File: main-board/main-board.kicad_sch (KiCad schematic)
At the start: 60 parts, among them J1 Conn_02x08_Odd_Even, J2 7-12V, Q1 2N7000, Q2 2N7000, Q3 2N7000, Q4 2N7000, Q5 2N7000, Q6 2N7000, Q7 2N7000, Q8 2N7000, Q9 2N3904, U1 40106, U2 4024, U3 4040, U4 27C256, U5 LM78L05, U6 ULN2803A, U7 4028, U9 L7805

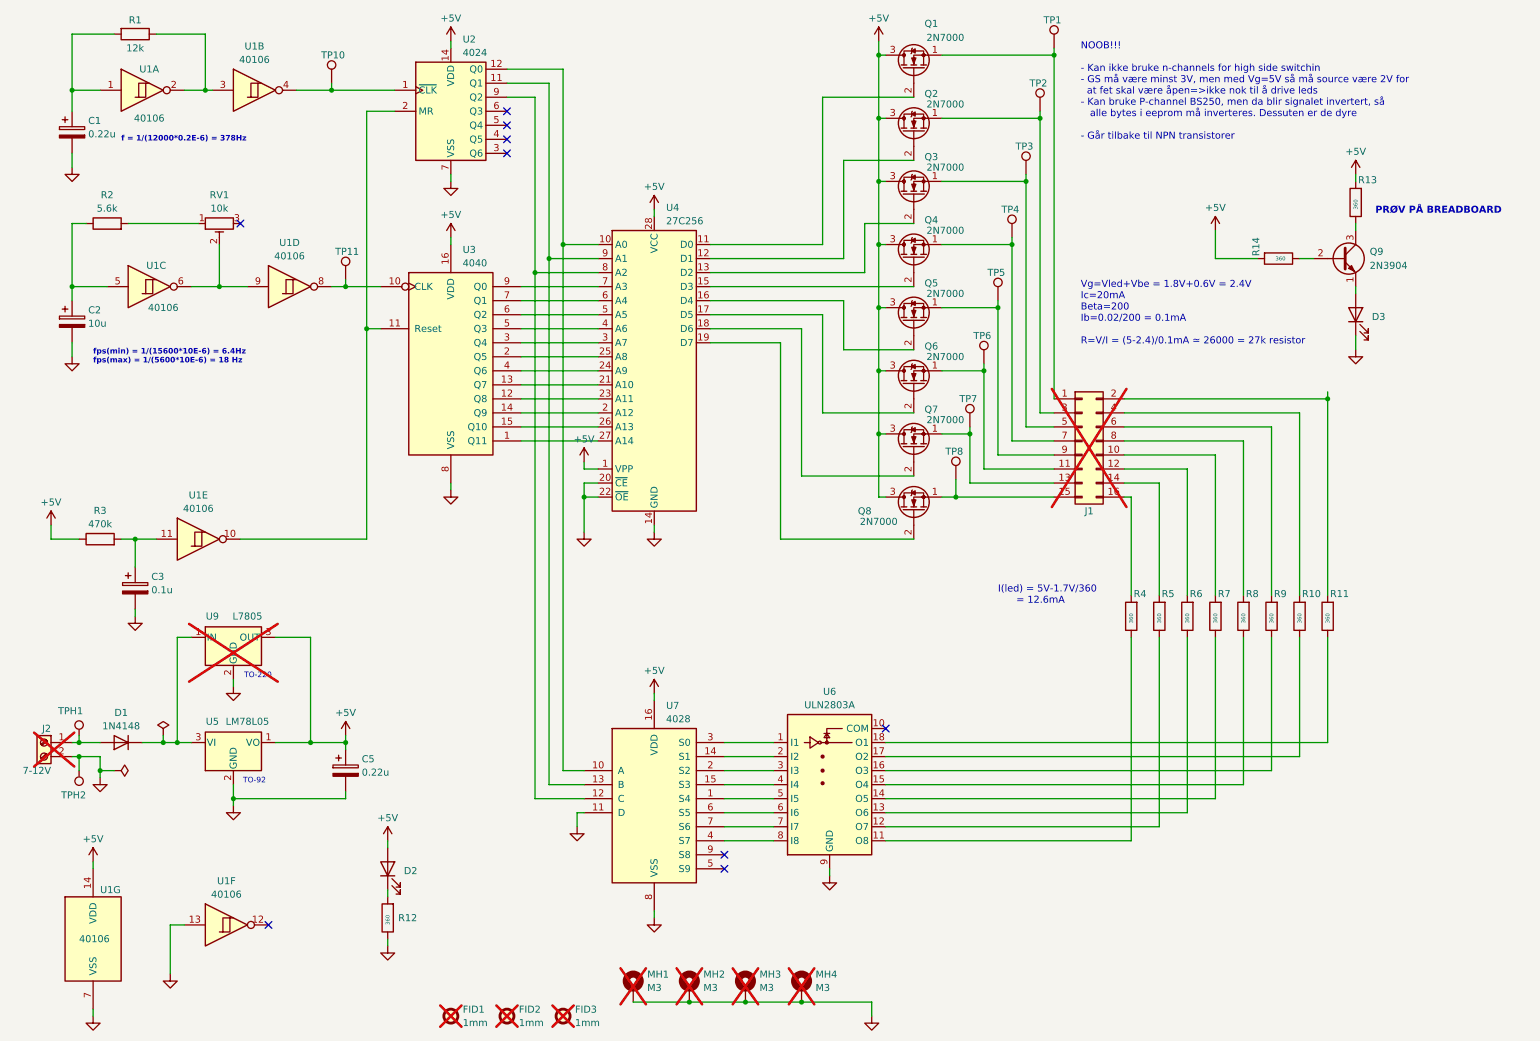
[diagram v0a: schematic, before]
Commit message: Started migrating to SMD
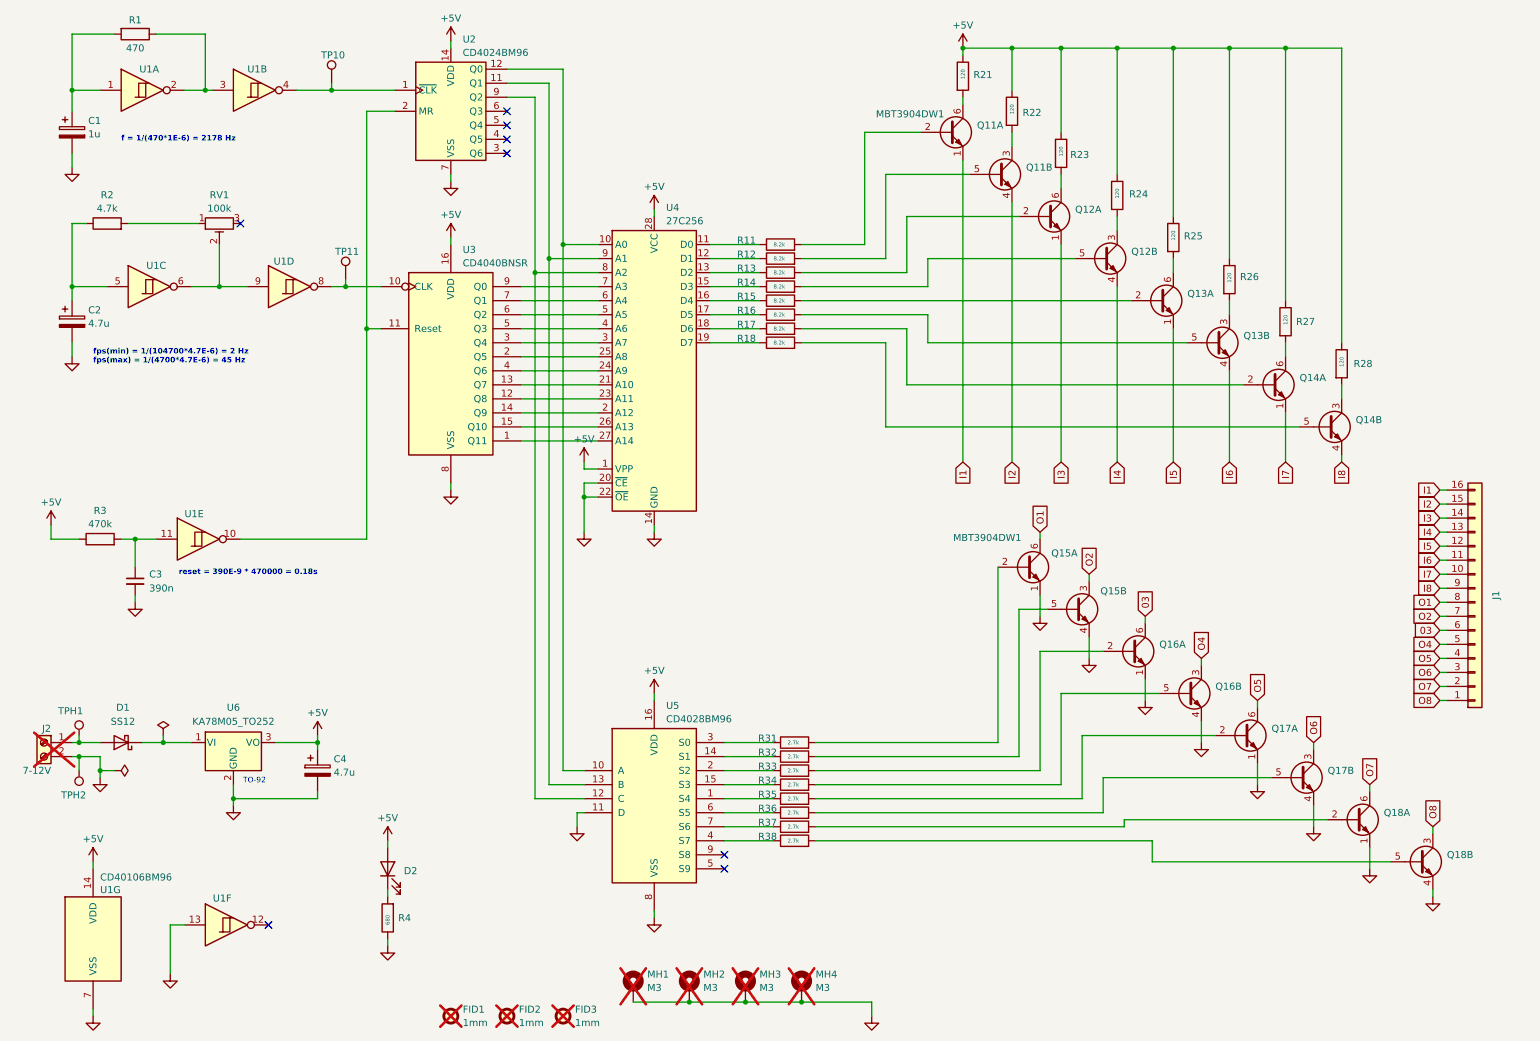
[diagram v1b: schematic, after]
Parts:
- removed C3: 0.1u, Capacitor_THT:CP_Radial_D4.0mm_P1.50mm, symbol Device:C_Polarized
- removed D1: 1N4148, Diode_THT:D_DO-35_SOD27_P7.62mm_Horizontal, symbol Diode:1N4148
- removed D3: LED, LED_THT:LED_D3.0mm, symbol Device:LED
- removed J1: Conn_02x08_Odd_Even, Connector_PinHeader_2.54mm:PinHeader_2x08_P2.54mm_Horizontal, symbol Connector_Generic:Conn_02x08_Odd_Even
- removed Q1, Q2, Q3, Q4, Q5, Q6, Q7, Q8: 2N7000, Package_TO_SOT_THT:TO-92_Inline, symbol Transistor_FET:2N7000
- removed Q9: 2N3904, Package_TO_SOT_THT:TO-92_Inline, symbol Transistor_BJT:2N3904
- removed R13, R14: 360, Resistor_THT:R_Axial_DIN0207_L6.3mm_D2.5mm_P10.16mm_Horizontal, symbol Device:R
- removed TP1, TP2, TP3, TP4, TP5, TP6, TP7, TP8: TestPoint, ezee-footprints:TestPoint_Pad_D1.0mm, symbol Connector:TestPoint
- removed U5: LM78L05, Package_TO_SOT_THT:TO-92_Inline, symbol Regulator_Linear:LM78L05_TO92
- removed U6: ULN2803A, Package_DIP:DIP-18_W7.62mm, symbol Transistor_Array:ULN2803A
- removed U9: L7805, Package_TO_SOT_THT:TO-220-3_Vertical, symbol Regulator_Linear:L7805
- added C3: 390n, Capacitor_SMD:C_0805_2012Metric, symbol Device:C_Small
- added D1: SS12, Diode_SMD:D_SMA, symbol Diode:SS12
- added J1: 16-bit, Connector_FFC-FPC:Molex_200528-0160_1x16-1MP_P1.00mm_Horizontal, symbol Connector_Generic:Conn_01x16
- added Q11, Q12, Q13, Q14, Q15, Q16, Q17, Q18: MBT3904DW1, Package_TO_SOT_SMD:SOT-363_SC-70-6, symbol Transistor_BJT:MBT3904DW1
- added R21, R22, R23, R24, R25, R26, R27, R28: 120, Resistor_SMD:R_0805_2012Metric, symbol Device:R
- added R31, R32, R33, R34, R35, R36, R37, R38: 2.7k, Resistor_SMD:R_0805_2012Metric, symbol Device:R
- added U6: KA78M05_TO252, Package_TO_SOT_SMD:TO-252-2, symbol Regulator_Linear:KA78M05_TO252
- C1: value 0.22u -> 1u; footprint Capacitor_THT:CP_Radial_D4.0mm_P1.50mm -> Capacitor_Tantalum_SMD:CP_EIA-6032-15_Kemet-U
- C2: value 10u -> 4.7u; footprint Capacitor_THT:CP_Radial_D4.0mm_P1.50mm -> Capacitor_Tantalum_SMD:CP_EIA-6032-15_Kemet-U
- C4: renamed from C5; value 0.22u -> 4.7u; footprint Capacitor_THT:CP_Radial_D4.0mm_P1.50mm -> Capacitor_Tantalum_SMD:CP_EIA-6032-15_Kemet-U
- D2: footprint LED_THT:LED_D3.0mm -> Inductor_SMD:L_1206_3216Metric
- R1: value 12k -> 470; footprint Resistor_THT:R_Axial_DIN0207_L6.3mm_D2.5mm_P10.16mm_Horizontal -> Resistor_SMD:R_0805_2012Metric
- R11: renamed from R4; value 360 -> 8.2k; footprint Resistor_THT:R_Axial_DIN0207_L6.3mm_D2.5mm_P10.16mm_Horizontal -> Resistor_SMD:R_0805_2012Metric
- R12: renamed from R5; value 360 -> 8.2k; footprint Resistor_THT:R_Axial_DIN0207_L6.3mm_D2.5mm_P10.16mm_Horizontal -> Resistor_SMD:R_0805_2012Metric
- R13: renamed from R6; value 360 -> 8.2k; footprint Resistor_THT:R_Axial_DIN0207_L6.3mm_D2.5mm_P10.16mm_Horizontal -> Resistor_SMD:R_0805_2012Metric
- R14: renamed from R7; value 360 -> 8.2k; footprint Resistor_THT:R_Axial_DIN0207_L6.3mm_D2.5mm_P10.16mm_Horizontal -> Resistor_SMD:R_0805_2012Metric
- R15: renamed from R8; value 360 -> 8.2k; footprint Resistor_THT:R_Axial_DIN0207_L6.3mm_D2.5mm_P10.16mm_Horizontal -> Resistor_SMD:R_0805_2012Metric
- R16: renamed from R9; value 360 -> 8.2k; footprint Resistor_THT:R_Axial_DIN0207_L6.3mm_D2.5mm_P10.16mm_Horizontal -> Resistor_SMD:R_0805_2012Metric
- R17: renamed from R10; value 360 -> 8.2k; footprint Resistor_THT:R_Axial_DIN0207_L6.3mm_D2.5mm_P10.16mm_Horizontal -> Resistor_SMD:R_0805_2012Metric
- R18: renamed from R11; value 360 -> 8.2k; footprint Resistor_THT:R_Axial_DIN0207_L6.3mm_D2.5mm_P10.16mm_Horizontal -> Resistor_SMD:R_0805_2012Metric
- R2: value 5.6k -> 4.7k; footprint Resistor_THT:R_Axial_DIN0207_L6.3mm_D2.5mm_P10.16mm_Horizontal -> Resistor_SMD:R_0805_2012Metric
- R3: footprint Resistor_THT:R_Axial_DIN0207_L6.3mm_D2.5mm_P10.16mm_Horizontal -> Resistor_SMD:R_0805_2012Metric
- R4: renamed from R12; value 360 -> 680; footprint Resistor_THT:R_Axial_DIN0207_L6.3mm_D2.5mm_P10.16mm_Horizontal -> Resistor_SMD:R_0805_2012Metric
- RV1: value 10k -> 100k
- U1: value 40106 -> CD40106BM96; footprint Package_DIP:DIP-14_W7.62mm -> Package_SO:SOIC-14_3.9x8.7mm_P1.27mm
- U2: value 4024 -> CD4024BM96; footprint Package_DIP:DIP-14_W7.62mm -> Package_SO:SOIC-14_3.9x8.7mm_P1.27mm
- U3: value 4040 -> CD4040BNSR; footprint Package_DIP:DIP-16_W7.62mm -> Package_SO:SOP-16_4.4x10.4mm_P1.27mm
- U5: renamed from U7; value 4028 -> CD4028BM96; footprint Package_DIP:DIP-16_W7.62mm -> Package_SO:SOIC-16W_5.3x10.2mm_P1.27mm
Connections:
- net +5V: now also R21.1, R22.1, R23.1, R24.1, R25.1, R26.1, R27.1, R28.1, U6.3 (VO)
- net GND: now also C3.2, Q15.1 (E1), Q15.4 (E2), Q16.1 (E1), Q16.4 (E2), Q17.1 (E1), Q17.4 (E2), Q18.1 (E1), Q18.4 (E2), U6.2 (GND)
- net at U4.13 (D2): now also R13.1
- net at R14.1: now also U4.15 (D3)
- net at R14.2: now also Q12.5 (B2)
- net at R13.2: now also Q12.2 (B1)
- net at R3.2, U1.11: now also C3.1
- net at U4.11 (D0): now also R11.1
- net at U4.12 (D1): now also R12.1
- net at U4.16 (D4): now also R15.1
- net at U4.17 (D5): now also R16.1
- net at U4.18 (D6): now also R17.1
- net at U4.19 (D7): now also R18.1
- net at R11.2: now also Q11.2 (B1)
- net at J2.1 (Pin_1), TPH1.1: now also D1.2 (A)
- net at R18.2: now also Q14.5 (B2)
- net at R12.2: now also Q11.5 (B2)
- net at R15.2: now also Q13.2 (B1)
- net at U5.1 (S4): now also R35.1
- net at U5.14 (S1): now also R32.1
- net at U5.15 (S3): now also R34.1
- net at U5.2 (S2): now also R33.1
- net at U5.3 (S0): now also R31.1
- net at U5.4 (S7): now also R38.1
- net at U5.6 (S5): now also R36.1
- net at U5.7 (S6): now also R37.1
- net at R16.2: now also Q13.5 (B2)
- net at R17.2: now also Q14.2 (B1)
- new net: Q11.6 (C1), R21.2
- new net: Q14.6 (C1), R27.2
- new net: D1.1 (K), U6.1 (VI)
- new net: Q16.5 (B2), R34.2
- new net: Q17.5 (B2), R36.2
- new net: Q16.2 (B1), R33.2
- new net: Q15.2 (B1), R31.2
- new net: Q12.6 (C1), R23.2
- new net: Q18.2 (B1), R37.2
- new net: Q13.3 (C2), R26.2
- new net: Q14.3 (C2), R28.2
- new net: Q13.6 (C1), R25.2
- new net: Q11.3 (C2), R22.2
- new net: Q17.2 (B1), R35.2
- new net: Q15.5 (B2), R32.2
- new net: Q18.5 (B2), R38.2
- new net: Q12.3 (C2), R24.2
- new net 03: J1.6 (Pin_6), Q16.6 (C1)
- new net I1: J1.16 (Pin_16), Q11.1 (E1)
- new net I2: J1.15 (Pin_15), Q11.4 (E2)
- new net I3: J1.14 (Pin_14), Q12.1 (E1)
- new net I4: J1.13 (Pin_13), Q12.4 (E2)
- new net I5: J1.12 (Pin_12), Q13.1 (E1)
- new net I6: J1.11 (Pin_11), Q13.4 (E2)
- new net I7: J1.10 (Pin_10), Q14.1 (E1)
- new net I8: J1.9 (Pin_9), Q14.4 (E2)
- new net O1: J1.8 (Pin_8), Q15.6 (C1)
- new net O2: J1.7 (Pin_7), Q15.3 (C2)
- new net O4: J1.5 (Pin_5), Q16.3 (C2)
- new net O5: J1.4 (Pin_4), Q17.6 (C1)
- new net O6: J1.3 (Pin_3), Q17.3 (C2)
- new net O7: J1.2 (Pin_2), Q18.6 (C1)
- new net O8: J1.1 (Pin_1), Q18.3 (C2)
- no-connect marks 9 -> 8
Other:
- note added: "f = 1/(470*1E-6) = 2178 Hz"
- note added: "fps(min) = 1/(104700*4.7E-6) = 2 Hz fps(max) = 1/(4700*4.7E-6) = 45 Hz"
- note added: "reset = 390E-9 * 470000 = 0.18s"
- note removed: "I(led) = 5V-1.7V/360 = 12.6mA"
- note removed: "NOOB!!! - Kan ikke bruke n-channels for high side switchin - GS må være minst 3V, men med Vg=5V så må source være 2V for at fet skal være åpen=>ikke nok til å drive leds - Kan bruke P-channel BS250, men da blir signalet invertert, så alle bytes i eeprom må inverteres. Dessuten er de dyre - Går tilbake til NPN transistorer"
- note removed: "PRØV PÅ BREADBOARD"
- note removed: "TO-220"
- note removed: "Vg=Vled+Vbe = 1.8V+0.6V = 2.4V Ic=20mA Beta=200 Ib=0.02/200 = 0.1mA R=V/I = (5-2.4)/0.1mA ≃ 26000 = 27k resistor"
- note removed: "f = 1/(12000*0.2E-6) = 378Hz"
- note removed: "fps(min) = 1/(15600*10E-6) = 6.4Hz fps(max) = 1/(5600*10E-6) = 18 Hz"
- moved on the sheet: C4, R11, R12, R13, R14, R15, R16, R17, R18

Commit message: routing complete - ready for QA
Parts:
- J2: footprint ezee-footprints:Battery_Terminals -> kicad-ezee-footprints:Battery_Terminals
- RV1: footprint ezee-footprints:Potentiometer_Wheel_3pin_Pitch4mm -> kicad-ezee-footprints:Potentiometer_Wheel_3pin_Pitch4mm
- TP10, TP11: footprint ezee-footprints:TestPoint_Pad_D1.0mm -> kicad-ezee-footprints:TestPoint_Pad_D1.0mm
- TPH1, TPH2: footprint ezee-footprints:TestPoint_Hook -> kicad-ezee-footprints:TestPoint_Hook; symbol ezee-symbols:TestPoint_Hook -> kicad-ezee-symbols:TestPoint_Hook; now in the parts list
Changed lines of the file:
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@@
 	)
 	(symbol
-		(lib_id "ezee-symbols:TestPoint_Hook")
+		(lib_id "kicad-ezee-symbols:TestPoint_Hook")
 		(at 26.67 149.86 180)
 		(unit 1)
 		(body_style 1)
 		(exclude_from_sim no)
-		(in_bom no)
+		(in_bom yes)
 		(on_board yes)
 		(in_pos_files yes)
@@
 			)
 		)
-		(property "Footprint" "ezee-footprints:TestPoint_Hook"
+		(property "Footprint" "kicad-ezee-footprints:TestPoint_Hook"
 			(at 21.717 147.32 0)
 			(hide yes)
@@
 			)
 		)
-		(property "Footprint" "ezee-footprints:TestPoint_Pad_D1.0mm"
+		(property "Footprint" "kicad-ezee-footprints:TestPoint_Pad_D1.0mm"
 			(at 80.01 60.96 0)
 			(hide yes)
@@
 			)
 		)
-		(property "Footprint" "ezee-footprints:Battery_Terminals"
+		(property "Footprint" "kicad-ezee-footprints:Battery_Terminals"
 			(at 20.32 144.78 0)
 			(hide yes)
@@
 	)
 	(symbol
-		(lib_id "ezee-symbols:TestPoint_Hook")
+		(lib_id "kicad-ezee-symbols:TestPoint_Hook")
 		(at 26.67 143.51 0)
 		(unit 1)
 		(body_style 1)
 		(exclude_from_sim no)
-		(in_bom no)
+		(in_bom yes)
 		(on_board yes)
 		(in_pos_files yes)
@@
 			)
 		)
-		(property "Footprint" "ezee-footprints:TestPoint_Hook"
+		(property "Footprint" "kicad-ezee-footprints:TestPoint_Hook"
 			(at 31.623 146.05 0)
 			(hide yes)
@@
 			)
 		)
-		(property "Footprint" "ezee-footprints:Potentiometer_Wheel_3pin_Pitch4mm"
+		(property "Footprint" "kicad-ezee-footprints:Potentiometer_Wheel_3pin_Pitch4mm"
 			(at 52.07 50.8 0)
 			(hide yes)
@@
 			)
 		)
-		(property "Footprint" "ezee-footprints:TestPoint_Pad_D1.0mm"
+		(property "Footprint" "kicad-ezee-footprints:TestPoint_Pad_D1.0mm"
 			(at 77.47 25.4 0)
 			(hide yes)
